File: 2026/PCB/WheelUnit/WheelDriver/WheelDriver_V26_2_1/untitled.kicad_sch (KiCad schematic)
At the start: 76 parts, among them J1 Conn_01x07_Pin, J2 Conn_01x02_Pin, J3 Conn_01x06_Socket, J4 Conn_01x03_Socket, J5 Conn_01x02_Socket, SW1 SW_MEC_5E, SW2 SW_MEC_5E, U1 MAX3051

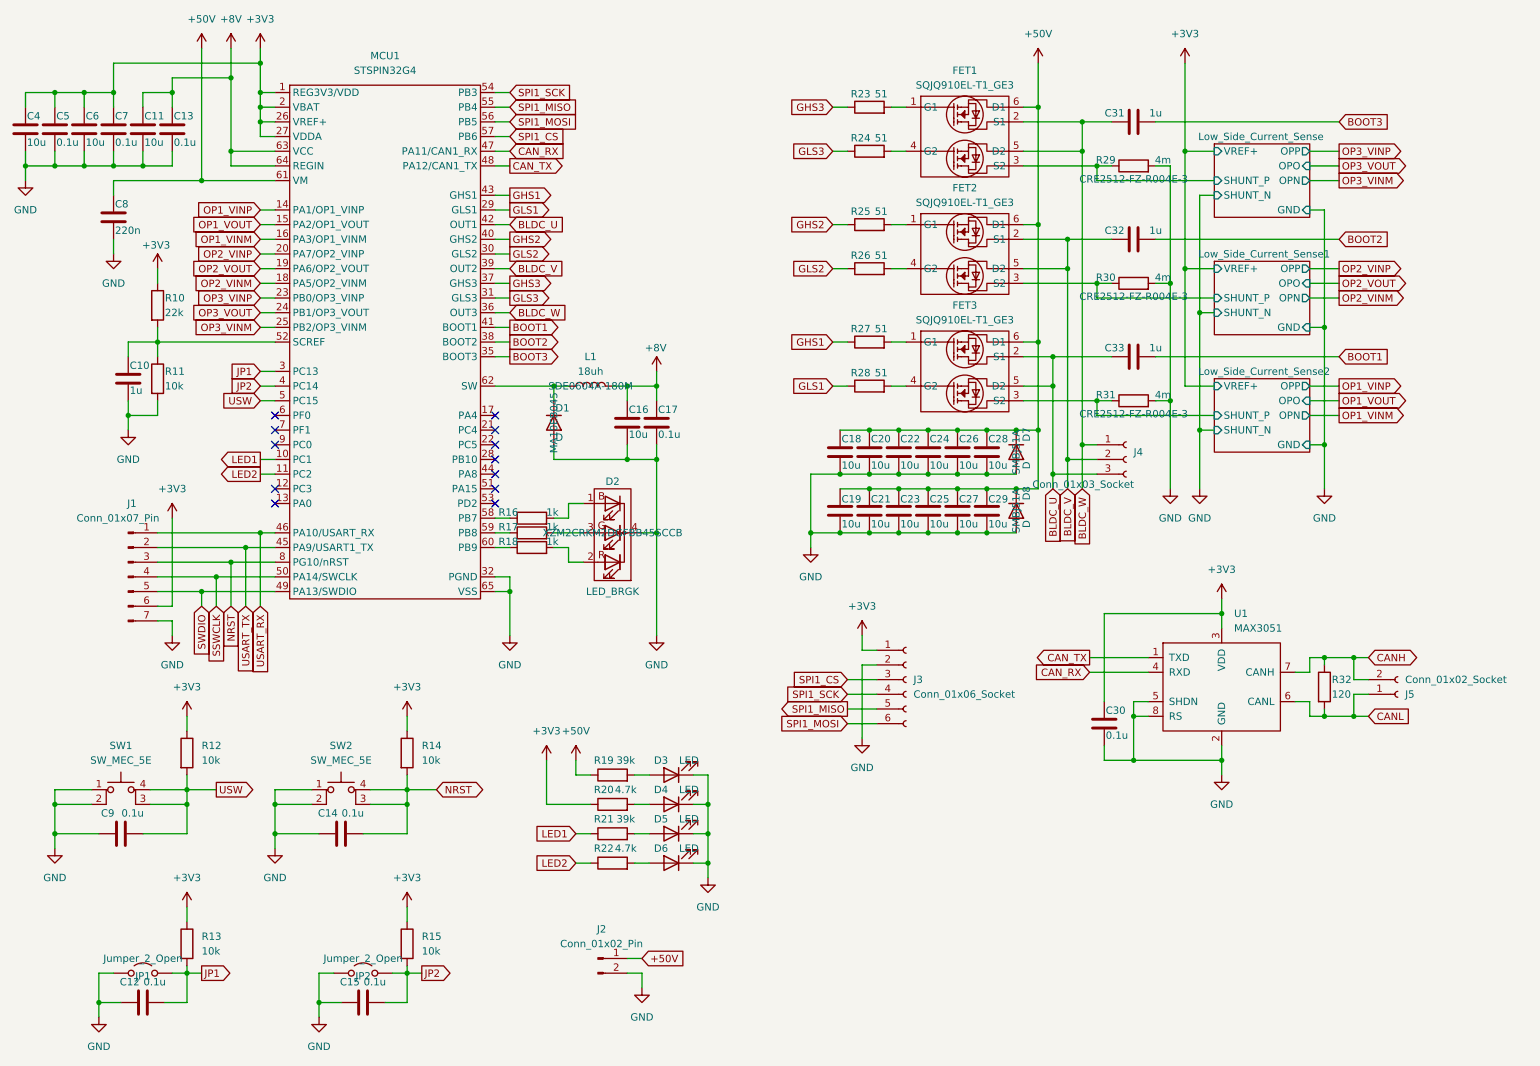
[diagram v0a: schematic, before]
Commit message: ジャンパーピン削除
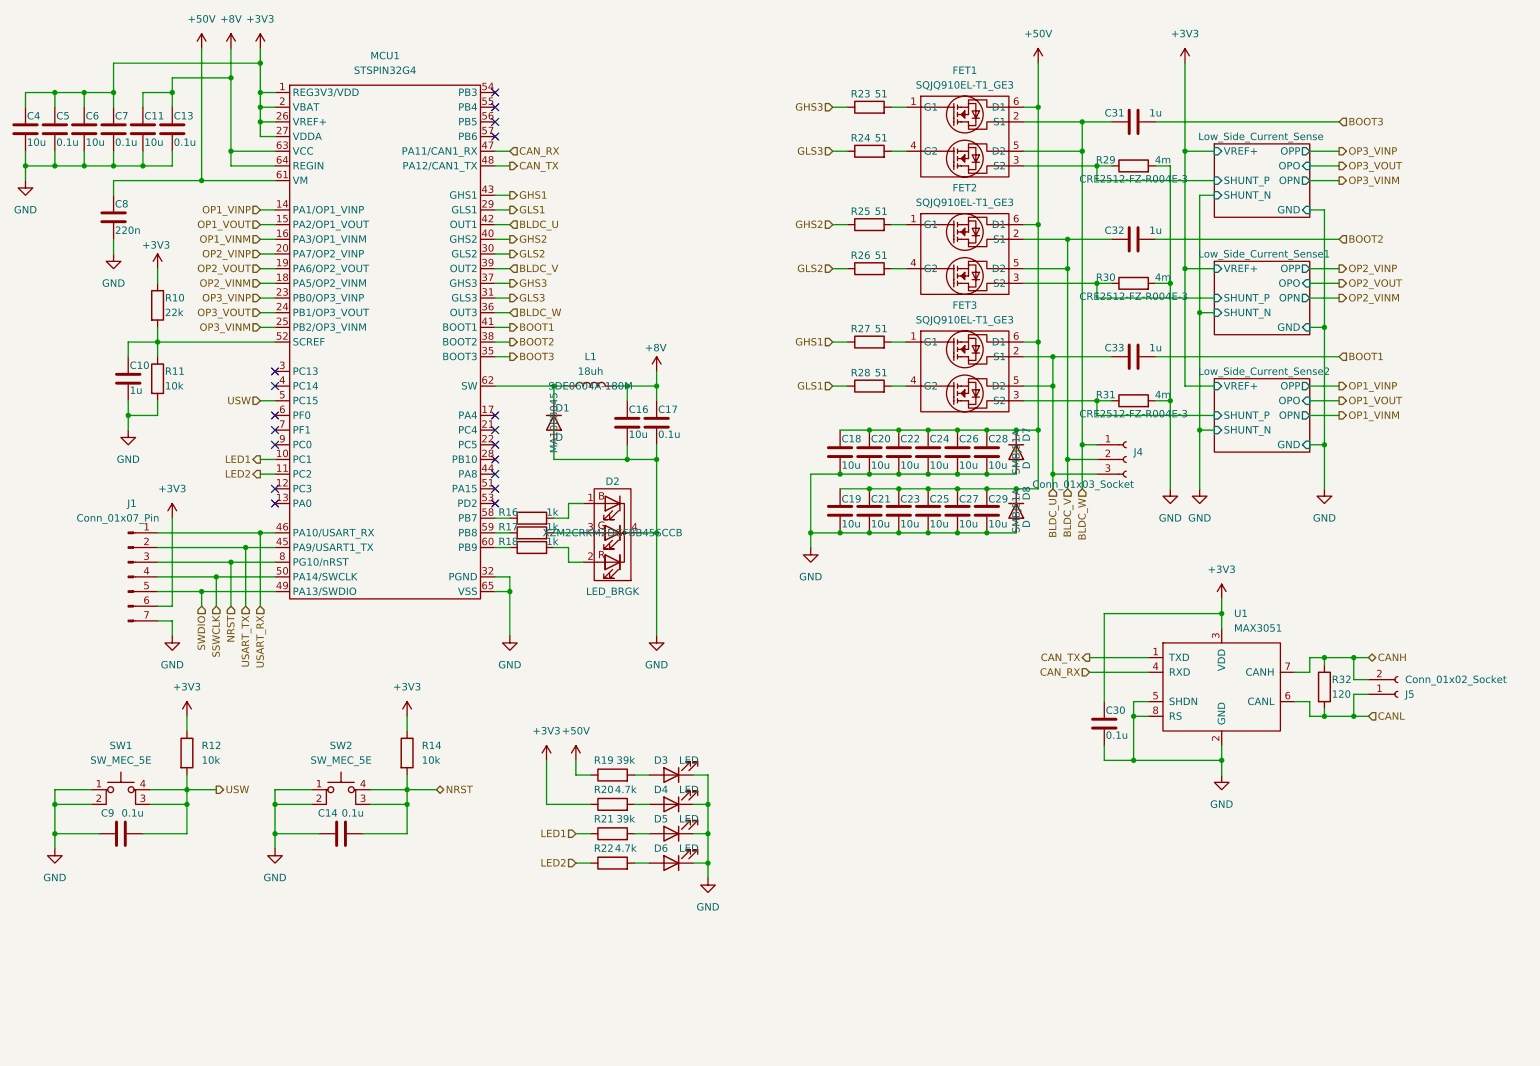
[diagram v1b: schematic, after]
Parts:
- removed C12, C15: 0.1u, Capacitor_SMD:C_0402_1005Metric_Pad0.74x0.62mm_HandSolder, symbol Device:C
- removed J2: Conn_01x02_Pin, Connector_Molex:Molex_SPOX_5268-02A_1x02_P2.50mm_Horizontal, symbol Connector:Conn_01x02_Pin
- removed J3: Conn_01x06_Socket, Connector_JST:JST_PH_S6B-PH-K_1x06_P2.00mm_Horizontal, symbol Connector:Conn_01x06_Socket
- removed JP1, JP2: Jumper_2_Open, Jumper:SolderJumper-2_P1.3mm_Open_TrianglePad1.0x1.5mm, symbol Jumper:Jumper_2_Open
- removed R13, R15: 10k, Resistor_SMD:R_0402_1005Metric_Pad0.72x0.64mm_HandSolder, symbol Device:R
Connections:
- net JP1: no longer names the net of MCU1.3 (PC13)
- net JP2: no longer names the net of MCU1.4 (PC14)
- net SPI1_CS: no longer names the net of MCU1.57 (PB6)
- net SPI1_MISO: no longer names the net of MCU1.55 (PB4)
- net SPI1_MOSI: no longer names the net of MCU1.56 (PB5)
- net SPI1_SCK: no longer names the net of MCU1.54 (PB3)
- no-connect marks 12 -> 18

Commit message: 回路図4ch化
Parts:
- removed D3: LED, BLDCUint_LIB_FTP:LED_1608_user_dif, symbol Device:LED
- removed FET1, FET2, FET3: SQJQ910EL-T1_GE3, BLDCUint_LIB_FTP:SQJQ910EL-T1_GE3, symbol BLDCUnit_LIB_SYM:SQJQ910EL-T1_GE3
- removed J1: Conn_01x07_Pin, Connector_JST:JST_PH_S7B-PH-K_1x07_P2.00mm_Horizontal, symbol Connector:Conn_01x07_Pin
- removed J4: Conn_01x03_Socket, Connector_Molex:Molex_SPOX_5268-03A_1x03_P2.50mm_Horizontal, symbol Connector:Conn_01x03_Socket
- removed J5: Conn_01x02_Socket, Connector_JST:JST_PH_S2B-PH-K_1x02_P2.00mm_Horizontal, symbol Connector:Conn_01x02_Socket
- removed R19: 39k, Resistor_SMD:R_0402_1005Metric_Pad0.72x0.64mm_HandSolder, symbol Device:R
- added FET1, FET2, FET3: SQJQ910EL-T1_GE3, symbol WheelUnit_LIB_SYM:SQJQ910EL-T1_GE3
- R25: renamed from R20; value 4.7k -> 1K
- R26: renamed from R21; value 39k -> 1K
- R27: renamed from R22; value 4.7k -> 1K
- renumbered C13 to C12, C14 to C13, C16 to C14, C17 to C15, C18 to C16, C19 to C17, C20 to C18, C21 to C19, C22 to C20, C23 to C21, C24 to C22, C25 to C23, C26 to C24, C27 to C25, C28 to C26, C29 to C27, C30 to C28, C31 to C29, C32 to C30, C33 to C31, C9 to C7, C7 to C8, C8 to C9, D7 to D10, D8 to D11, D1 to D5, D2 to D6, D4 to D7, D5 to D8, D6 to D9, R10 to R18, R11 to R19, R12 to R20, R14 to R21, R16 to R22, R17 to R23, R18 to R24, R23 to R28, R24 to R29, R25 to R30, R26 to R31, R27 to R32, R28 to R33, R29 to R34, R30 to R35, R31 to R36, R32 to R37, SW1 to SW2, SW2 to SW3, U1 to U7
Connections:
- net +3V3: no longer R25.1
- net +50V: now also FET1.6 (D1), FET2.6 (D1), FET3.6 (D1)
- net BLDC_U: now also FET3.2 (S1), FET3.5 (D2)
- net BLDC_V: now also FET2.2 (S1), FET2.5 (D2)
- net BLDC_W: now also FET1.2 (S1), FET1.5 (D2)
- net Low_Side_Current_Sense/SHUNT_P: now also FET1.3 (S2)
- net Low_Side_Current_Sense1/SHUNT_P: now also FET2.3 (S2)
- net Low_Side_Current_Sense2/SHUNT_P: now also FET3.3 (S2)
- net NRST: now also C7.1, R20.2, SW2.3 (K), SW2.4 (A); no longer C13.1, R21.2, SW3.3 (K), SW3.4 (A)
- net USW: now also C13.1, R21.2, SW3.3 (K), SW3.4 (A); no longer C7.1, R20.2, SW2.3 (K), SW2.4 (A)
- net at R31.2: now also FET2.4 (G2)
- net at R32.2: now also FET3.1 (G1)
- net at R33.2: now also FET3.4 (G2)
- net at R28.2: now also FET1.1 (G1)
- net at R29.2: now also FET1.4 (G2)
- net at R30.2: now also FET2.1 (G1)
- net LED_CAN: now reaches MCU1.12 (PC3)
- net LED_CAN: now also R25.1
- net ENC: now reaches MCU1.9 (PC0)
- net SSWCLK renamed SWCLK
- no-connect marks 18 -> 16
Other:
- moved on the sheet: C10, C11, C12, C13, C14, C15, C16, C17, C18, C19, C20, C21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

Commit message: 回路図終わり
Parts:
- removed D10, D11: D, Diode_SMD:D_SMB, symbol Device:D
- added D10, D11: SMAJ51A, Diode_SMD:D_SMA, symbol Diode:SMAJ51A
- C29, C30, C31: value 1u -> 2.2u; footprint Capacitor_SMD:C_0603_1608Metric_Pad1.08x0.95mm_HandSolder -> Capacitor_SMD:C_0805_2012Metric_Pad1.18x1.45mm_HandSolder
- D5: footprint BLDCUint_LIB_FTP:MA10EB045 -> WheelUnit_LIB_FTP:MA10EB045
- D7, D8, D9: footprint BLDCUint_LIB_FTP:LED_1608_user_dif -> WheelUnit_LIB_FTP:LED_1608_user_dif
- FET1, FET2, FET3: footprint (none) -> WheelUnit_LIB_FTP:SQJQ910EL-T1_GE3
- SW2, SW3: footprint BLDCUint_LIB_FTP:SW_SKRPACE010 -> WheelUnit_LIB_FTP:SW_SKRPACE010
- renumbered C8 to C7, C9 to C8, C7 to C9
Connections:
- net +50V: now also D10.1 (A1), D11.1 (A1)
- net BLDC_U: now also C29.1, FET1.2 (S1), FET1.5 (D2); no longer C31.1, FET3.2 (S1), FET3.5 (D2)
- net BLDC_W: now also C31.1, FET3.2 (S1), FET3.5 (D2); no longer C29.1, FET1.2 (S1), FET1.5 (D2)
- net GND: now also D10.2 (A2), D11.2 (A2)
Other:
- moved on the sheet: C13, C9, D7, D8, D9, R20, R21, R25, R26, R27, SW2, SW3

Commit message: ん、STPIN??周辺の配置だいたい終わり＆早く寝ましょう
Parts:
- D5: footprint WheelUnit_LIB_FTP:MA10EB045 -> Diode_SMD:D_SOD-123F
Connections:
- net USW: now also MCU1.3 (PC13); no longer MCU1.5 (PC15)
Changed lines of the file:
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@@
 	)
 	(no_connect
-		(at 68.58 81.28)
-	)
-	(no_connect
 		(at 106.68 40.64)
 	)
@@
 	)
 	(no_connect
+		(at 68.58 86.36)
+	)
+	(no_connect
 		(at 106.68 101.6)
 	)
@@
 	(wire
 		(pts
-			(xy 66.04 86.36) (xy 68.58 86.36)
+			(xy 66.04 81.28) (xy 68.58 81.28)
 		)
 		(stroke
@@
 	)
 	(label "USW"
-		(at 66.04 86.36 180)
+		(at 66.04 81.28 180)
 		(effects
 			(font
@@
 			)
 		)
-		(property "Footprint" "WheelUnit_LIB_FTP:MA10EB045"
+		(property "Footprint" "Diode_SMD:D_SOD-123F"
 			(at 116.84 90.17 0)
 			(effects
@@
 			)
 		)
-		(property "Description" "MA10EB045"
+		(property "Description" "SM5817PL-TP"
 			(at 116.84 90.17 0)
 			(effects

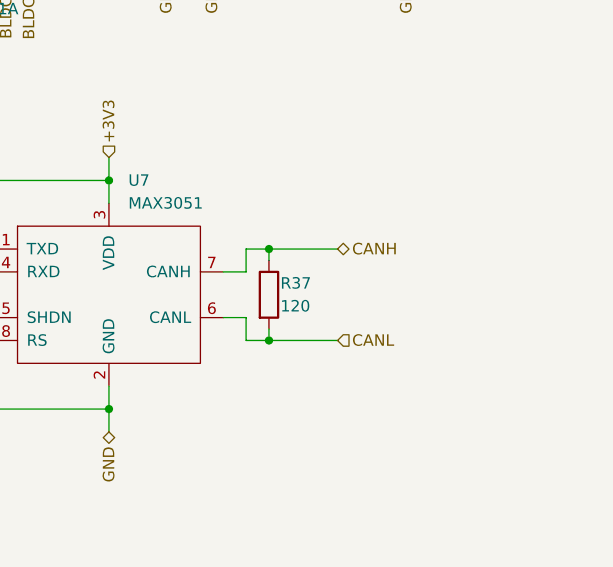
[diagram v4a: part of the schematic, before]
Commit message: コモンモードチョークコイル(DLW32SH101XF2L)追加
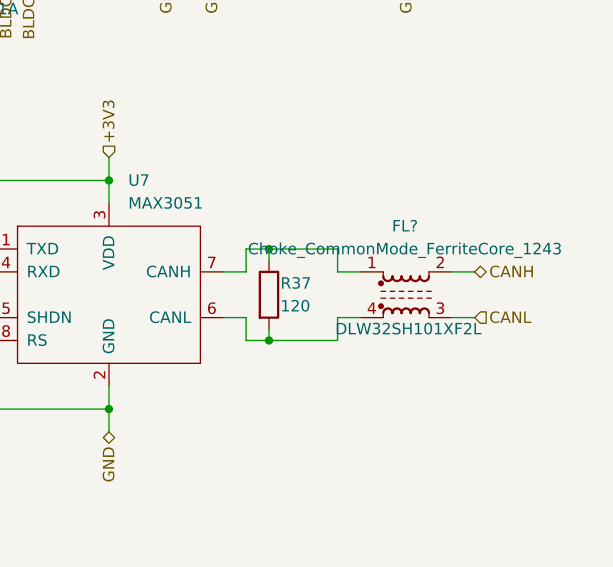
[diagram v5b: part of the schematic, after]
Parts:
- added FL?: Choke_CommonMode_FerriteCore_1243, symbol Filter:Choke_CommonMode_FerriteCore_1243
- MCU1: footprint Package_DFN_QFN:VQFN-64-1EP_9x9mm_P0.5mm_EP5.4x5.4mm -> WheelUnit_LIB_FTP:STSPIN32G4
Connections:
- net CANH: now also FL?.2; no longer R37.1, U7.7 (CANH)
- net CANL: now also FL?.3; no longer R37.2, U7.6 (CANL)
- new net: FL?.1, R37.1, U7.7 (CANH)
- new net: FL?.4, R37.2, U7.6 (CANL)
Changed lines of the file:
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@@
 	(wire
 		(pts
+			(xy 241.3 133.35) (xy 241.3 135.89)
+		)
+		(stroke
+			(width 0)
+			(type default)
+		)
+	)
+	(wire
+		(pts
 			(xy 66.04 38.1) (xy 68.58 38.1)
 		)
@@
 	(wire
 		(pts
+			(xy 241.3 143.51) (xy 241.3 140.97)
+		)
+		(stroke
+			(width 0)
+			(type default)
+		)
+	)
+	(wire
+		(pts
 			(xy 185.42 109.22) (xy 190.5 109.22)
 		)
@@
 	(wire
 		(pts
+			(xy 254 135.89) (xy 256.54 135.89)
+		)
+		(stroke
+			(width 0)
+			(type default)
+		)
+	)
+	(wire
+		(pts
 			(xy 246.38 63.5) (xy 251.46 63.5)
 		)
@@
 	(wire
 		(pts
+			(xy 241.3 140.97) (xy 243.84 140.97)
+		)
+		(stroke
+			(width 0)
+			(type default)
+		)
+	)
+	(wire
+		(pts
 			(xy 173.99 43.18) (xy 176.53 43.18)
 		)
@@
 	(wire
 		(pts
+			(xy 254 140.97) (xy 256.54 140.97)
+		)
+		(stroke
+			(width 0)
+			(type default)
+		)
+	)
+	(wire
+		(pts
 			(xy 195.58 151.13) (xy 200.66 151.13)
 		)
@@
 		)
 	)
+	(wire
+		(pts
+			(xy 241.3 135.89) (xy 243.84 135.89)
+		)
+		(stroke
+			(width 0)
+			(type default)
+		)
+	)
 	(label "NRST"
 		(at 58.42 160.02 0)
@@
 	(hierarchical_label "CANL"
 		(shape input)
-		(at 241.3 143.51 0)
+		(at 256.54 140.97 0)
 		(effects
 			(font
@@
 	(hierarchical_label "CANH"
 		(shape bidirectional)
-		(at 241.3 133.35 0)
+		(at 256.54 135.89 0)
 		(effects
 			(font
@@
 	)
 	(symbol
+		(lib_id "Filter:Choke_CommonMode_FerriteCore_1243")
+		(at 248.92 138.43 0)
+		(unit 1)
+		(exclude_from_sim no)
+		(in_bom yes)
+		(on_board yes)
+		(dnp no)
+		(property "Reference" "FL?"
+			(at 248.793 130.81 0)
+			(effects
+				(font
+					(size 1.27 1.27)
+				)
+			)
+		)
+		(property "Value" "Choke_CommonMode_FerriteCore_1243"
+			(at 248.793 133.35 0)
+			(effects
+				(font
+					(size 1.27 1.27)
+				)
+			)
+		)
+		(property "Footprint" ""
+			(at 248.92 144.78 0)
+			(effects
+				(font
+					(size 1.27 1.27)
+				)
+				(hide yes)
+			)
+		)
+		(property "Datasheet" "~"
+			(at 248.92 146.685 0)
+			(effects
+				(font
+					(size 1.27 1.27)
+				)
+				(hide yes)
+			)
+		)
+		(property "Description" "DLW32SH101XF2L"
+			(at 249.174 142.24 0)
+			(effects
+				(font
+					(size 1.27 1.27)
+				)
+			)
+		)
+		(pin "1"
+		)
+		(pin "4"
+		)
+		(pin "2"
+		)
+		(pin "3"
+		)
+		(instances
+			(project ""
+				(path "/b60d34e1-e978-4abb-befd-6af7b603dc53/01c53688-c3c5-4098-8cb1-7076c72bfd6c"
+					(reference "FL?")
+					(unit 1)
+				)
+			)
+		)
+	)
+	(symbol
 		(lib_id "Device:LED")
 		(at 135.89 157.48 180)
@@
 			)
 		)
-		(property "Footprint" "Package_DFN_QFN:VQFN-64-1EP_9x9mm_P0.5mm_EP5.4x5.4mm"
+		(property "Footprint" "WheelUnit_LIB_FTP:STSPIN32G4"
 			(at 87.63 76.2 0)
 			(effects

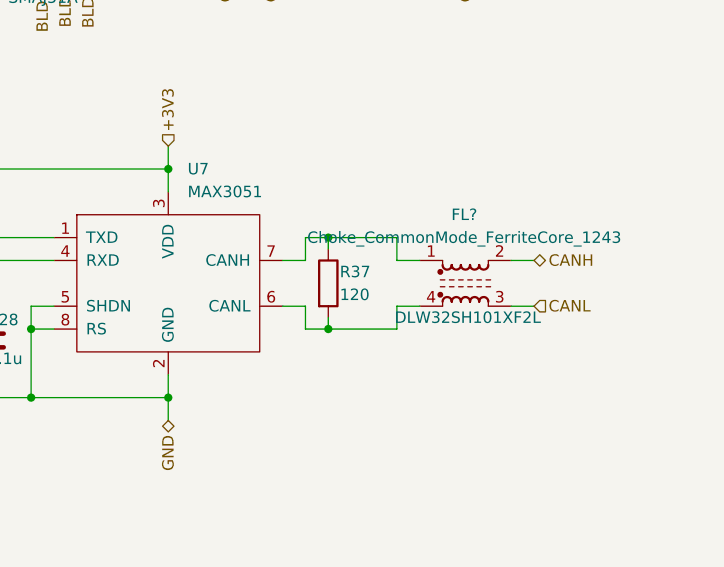
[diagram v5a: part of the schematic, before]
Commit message: CAN終端を分割終端方式に変更
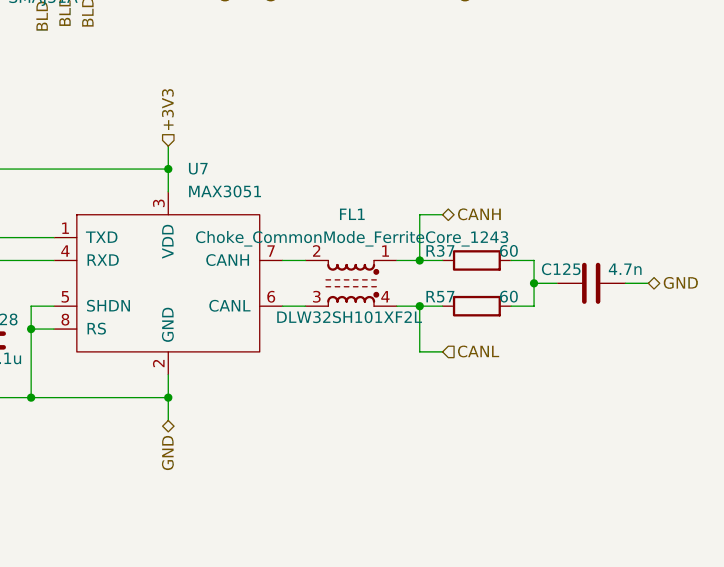
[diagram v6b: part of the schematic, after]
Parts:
- added C125: 4.7n, Capacitor_SMD:C_0603_1608Metric_Pad1.08x0.95mm_HandSolder, symbol Device:C
- added R57: 60, Resistor_SMD:R_0402_1005Metric_Pad0.72x0.64mm_HandSolder, symbol Device:R
- FL1: renamed from FL?; footprint (none) -> WheelUnit_LIB_FTP:FIL_DLW32SH101XF2L
- R37: value 120 -> 60; footprint Resistor_SMD:R_0603_1608Metric_Pad0.98x0.95mm_HandSolder -> Resistor_SMD:R_0402_1005Metric_Pad0.72x0.64mm_HandSolder
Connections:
- net CANH: now also FL1.1, R37.1; no longer FL1.2
- net CANL: now also FL1.4, R57.1; no longer FL1.3
- net GND: now also C125.2
- new net: FL1.2, U7.7 (CANH)
- new net: FL1.3, U7.6 (CANL)
- new net: C125.1, R37.2, R57.2
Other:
- moved on the sheet: FL1

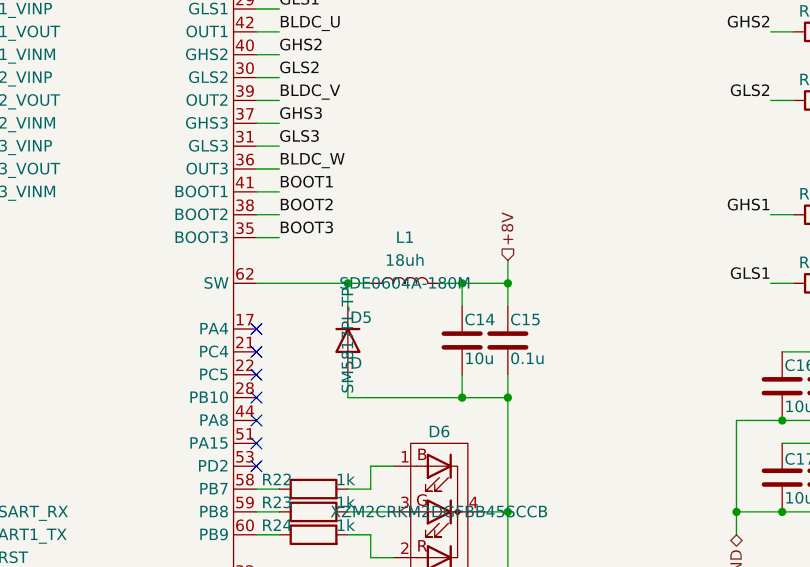
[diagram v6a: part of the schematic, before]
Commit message: 18uHのインダクタのFTP変更
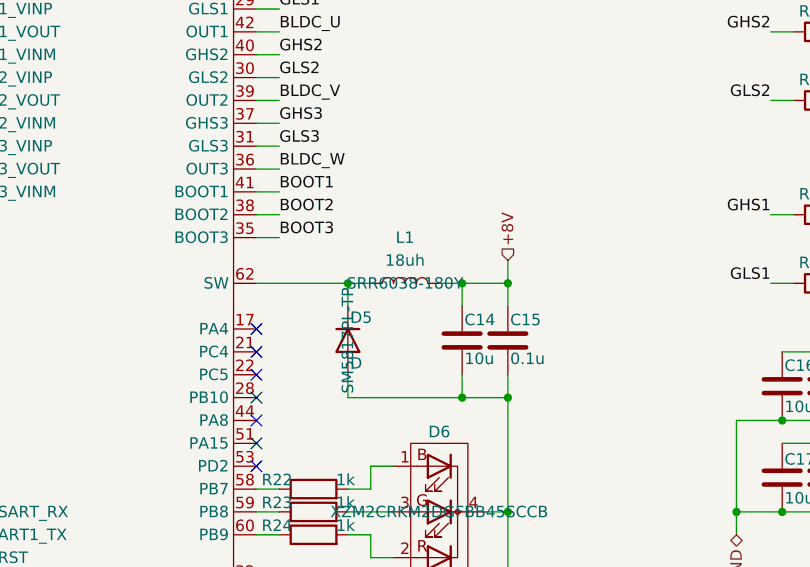
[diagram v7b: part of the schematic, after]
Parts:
- L1: footprint Inductor_SMD:L_Cenker_CKCS6020 -> WheelUnit_LIB_FTP:IND_SRR6038-180Y
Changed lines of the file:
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@@
 			)
 		)
-		(property "Footprint" "Inductor_SMD:L_Cenker_CKCS6020"
+		(property "Footprint" "WheelUnit_LIB_FTP:IND_SRR6038-180Y"
 			(at 123.19 83.82 0)
 			(effects
@@
 			)
 		)
-		(property "Description" "SDE0604A-180M"
+		(property "Description" "SRR6038-180Y"
 			(at 123.19 83.82 90)
 			(effects

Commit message: DIPSWを4chから2chに変更
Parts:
- SW2, SW3: footprint WheelUnit_LIB_FTP:SW_SKRPACE010 -> WheelUnit_LIB_FTP:SW_SKRPACE010_ud
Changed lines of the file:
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@@
 			)
 		)
-		(property "Footprint" "WheelUnit_LIB_FTP:SW_SKRPACE010"
+		(property "Footprint" "WheelUnit_LIB_FTP:SW_SKRPACE010_ud"
 			(at 80.01 154.94 0)
 			(effects
@@
 			)
 		)
-		(property "Footprint" "WheelUnit_LIB_FTP:SW_SKRPACE010"
+		(property "Footprint" "WheelUnit_LIB_FTP:SW_SKRPACE010_ud"
 			(at 41.91 154.94 0)
 			(effects
